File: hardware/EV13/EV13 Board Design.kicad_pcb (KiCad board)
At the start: 4 copper layers, 66 x 99.3 mm, 144 parts, among them CN2 Conn_05x02_Female, CN3 Conn_01x06_Female, CN4 Conn_01x06_Female, CN5 Conn_02x05_Male, CN6 Conn_02x05_Male, CN7 Conn_02x05_Male, J1 Conn_01x02_Socket, J10 Conn_01x08_Socket, J2 AudioJack1, J3 Conn_01x06_Socket, J9 USB_C_Receptacle, SW1 SW_Push, SW3 SW_Push, SW4 SW_Push, SW5 SW_Push, SW6 SW_SPDT, U1 STM32F405RGTx, U11 ESP32-S3-WROOM-1-N8R2, U13 BM14B(0.8)-24DS-0.4V(53), U2 BQ21040DBV, U3 CH340C, U4 USBLC6-2P6, U5 M24C02-RMN6TP, U6 WM8960CGEFL/RV, U7 TPS63060, U8 STM32F072CBTx, Y1 Crystal_GND24

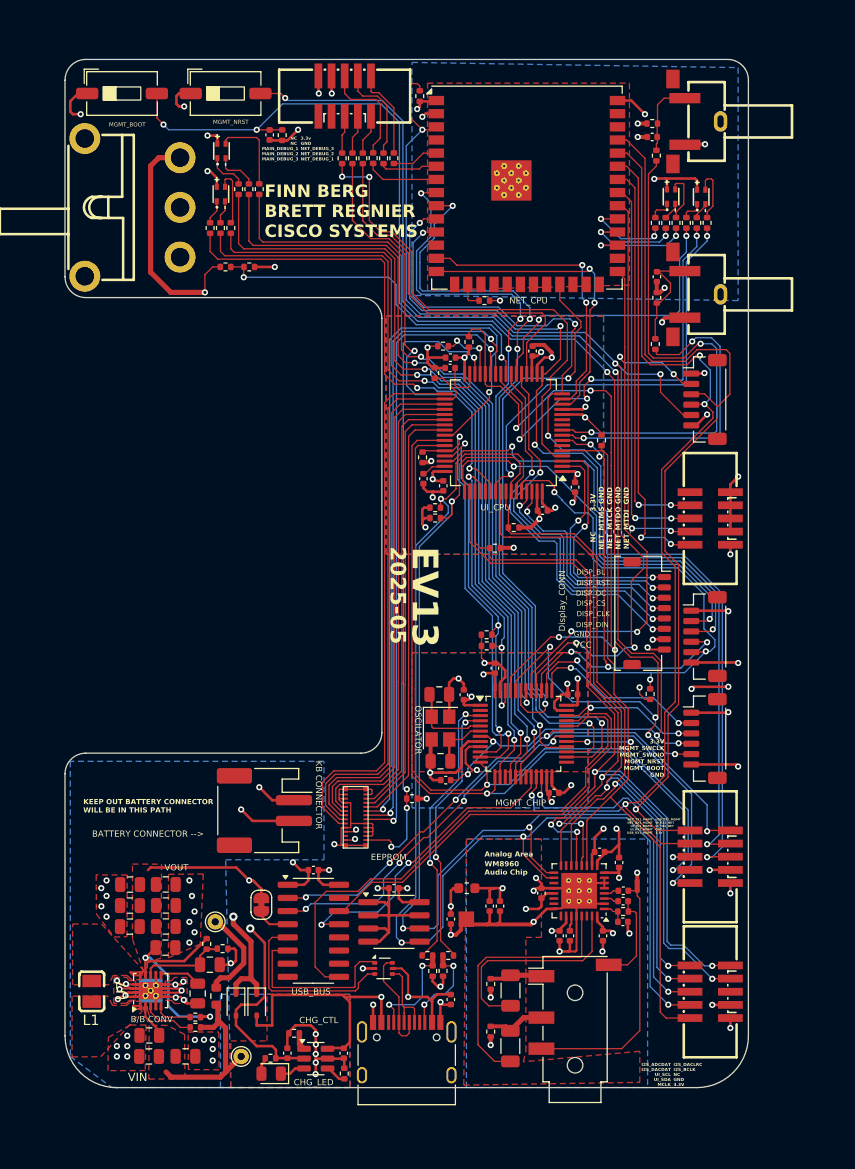
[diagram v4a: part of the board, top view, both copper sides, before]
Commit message: Resolved simple issues, switched wifi, moved KB connector
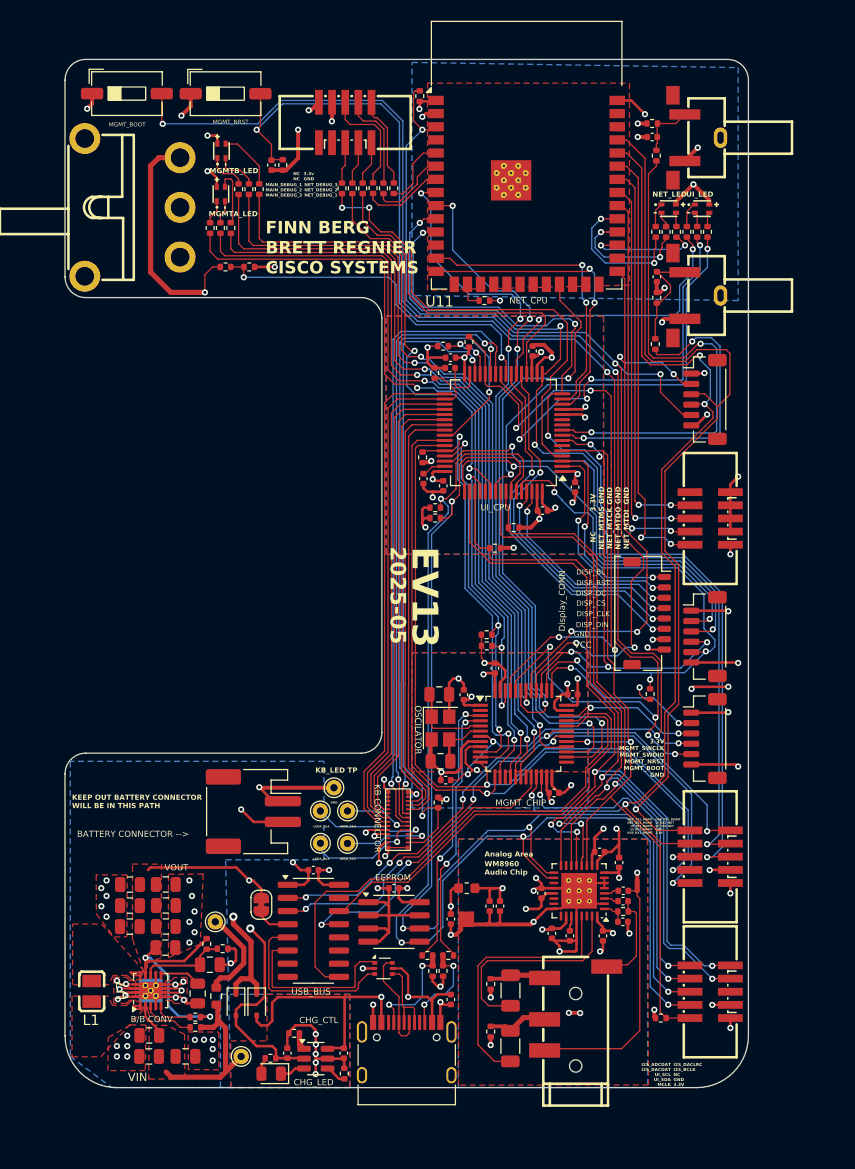
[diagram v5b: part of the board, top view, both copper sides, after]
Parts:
- added TP3: TestPoint, TestPoint:TestPoint_THTPad_D1.5mm_Drill0.7mm, F.Cu at (141.3, 118.6)
- added TP4: TestPoint, TestPoint:TestPoint_THTPad_D1.5mm_Drill0.7mm, F.Cu at (138.7, 118.6)
- added TP5: TestPoint, TestPoint:TestPoint_THTPad_D1.5mm_Drill0.7mm, F.Cu at (141.3, 121.7)
- added TP6: TestPoint, TestPoint:TestPoint_THTPad_D1.5mm_Drill0.7mm, F.Cu at (138.7, 121.7)
- added TP7: TestPoint, TestPoint:TestPoint_THTPad_D1.5mm_Drill0.7mm, F.Cu at (140.0, 116.3)
- C28, C31: value 4.7u -> 4u7
- J2: footprint Connector_Audio:Jack_3.5mm_PJ320D_Horizontal -> Hactar_Footprints:AUDIO-SMD_PJ-320D
- U11: value ESP32-S3-WROOM-1-N8R2 -> ESP32-S3-WROOM-1; footprint RF_Module:ESP32-S3-WROOM-1U -> RF_Module:ESP32-S3-WROOM-1
- moved R50 56.1 mm to (171.5, 138.6), turned to 0 degrees
- moved SW4 10.0 mm to (129.5, 49.3)
- moved SW5 9.53 mm to (120.0, 49.3)
- moved U13 4.10 mm to (147.4, 122.4)
- moved U11 3.16 mm to (158.6, 55.2)
- moved C36 2.93 mm to (133.9, 56.2)
- moved R37 2.90 mm to (144.8, 58.5)
- moved R39 2.90 mm to (140.8, 58.5)
- moved R40 2.90 mm to (141.8, 58.5)
- moved R41 2.90 mm to (142.8, 58.5)
- moved R36 2.90 mm to (143.8, 58.4)
- moved R38 2.90 mm to (145.8, 58.4)
- moved R10 2.88 mm to (135.0, 56.2)
- moved CN7 2.55 mm to (141.1, 52.1)
- moved R44 2.55 mm to (150.0, 117.8), turned to -90 degrees
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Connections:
- U13 pad 23: GND -> /KB_LEDK_2&3
- U13 pad 24: GND -> /KB_LEDA_3&4
- U13 pad 25: GND -> /KB_LEDK_1&4
- U13 pad 26: GND -> /KB_LEDA_1&2
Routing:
- net GND: track 648.8 -> 663.4 mm, vias 79 -> 83
- net +3.3V: track 512.7 -> 498.2 mm
- net /MGMT_NRST: track 122.1 -> 135.1 mm
- net /KB_LEDA_3&4: track 0.00 -> 11.1 mm, vias 0 -> 1
- net /KB_LEDK_1&4: track 0.00 -> 10.9 mm, vias 0 -> 1
- net GNDA: track 97.8 -> 107.1 mm, vias 10 -> 12
- net /KB_LEDA_1&2: track 0.00 -> 9.03 mm, vias 0 -> 1
- net /NET_CTS1_MGMT: track 76.5 -> 69.9 mm
- net /MGMT_BOOT: track 135.1 -> 128.5 mm, vias 7 -> 6
- net /KB_LEDK_2&3: track 0.00 -> 6.55 mm, vias 0 -> 1
- net /NET_LED_R: track 8.46 -> 13.9 mm
- net /KB_ROW4: track 70.8 -> 65.7 mm
- net Net-(D7---Pad3): track 5.55 -> 1.40 mm
- net /KB_COL3: track 47.6 -> 43.7 mm
- net /NET_RTS1_MGMT: track 75.2 -> 71.3 mm
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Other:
- board text added: "KB_LED TP"
- board text added: "LEDA_1&2"
- board text added: "LEDA_3&4"
- board text added: "LEDK_1&4"
- board text added: "LEDK_2&3"
- board text added: "MGMTA_LED"
- board text added: "MGMTB_LED"
- board text added: "NET_LED"
- board text added: "UI_LED"
